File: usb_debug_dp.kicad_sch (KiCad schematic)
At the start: 141 parts, among them J7 Tag-Connect_TC2050-IDC-NL_2x5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, J8 USB-C_GCT_USB4105-GF-A, J9 USB-C_Amphenol_12401598E4, Q12 PJE138K, U29 W25Q80DV_USON, U30 TPS65988DHRSHR, U31 NTS0102_XSON, U32 NCP730BMT330_WSON, U33 TUSB1046-DCIRNQ, U34 FT230X_QFN, U35 AP22615A_TSOT26, U36 TPD4E05U06QDQARQ1, U37 TPD4E05U06QDQARQ1, U38 TPD4E05U06QDQARQ1, U39 TPS65988DHRSHR, U40 AP22615A_TSOT26, U41 TPD4E05U06QDQARQ1, U42 TPD4E05U06QDQARQ1

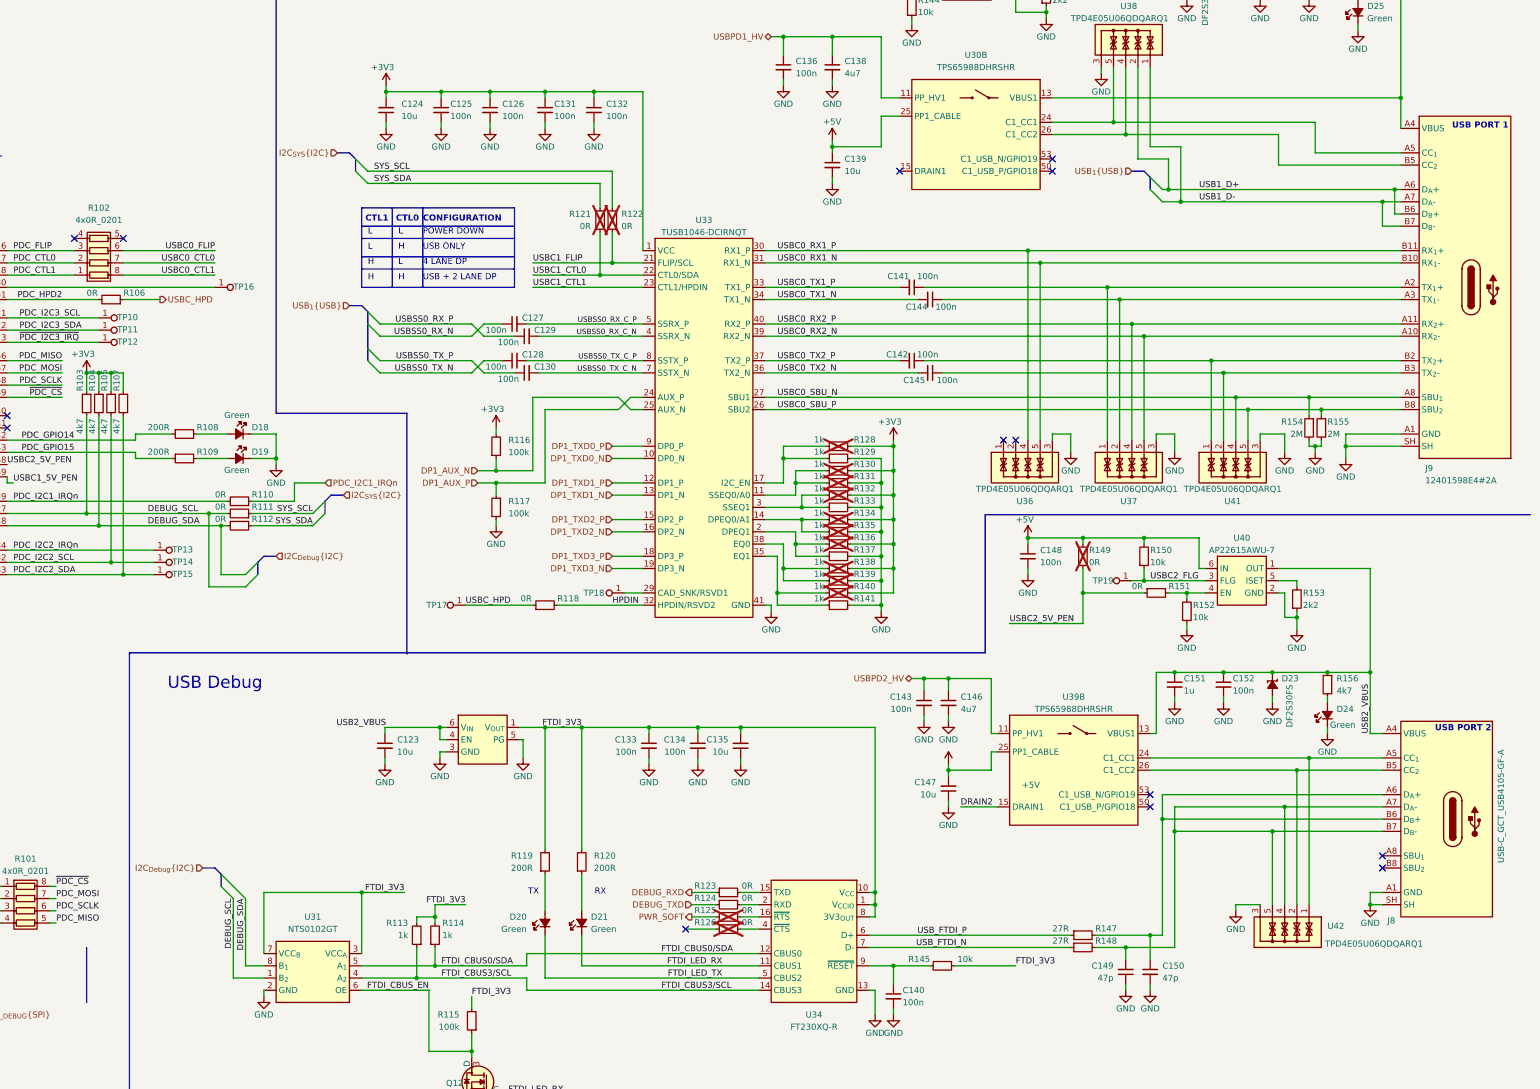
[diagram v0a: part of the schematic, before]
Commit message: [#82847] Prepare current state of schematic to merge with mockup
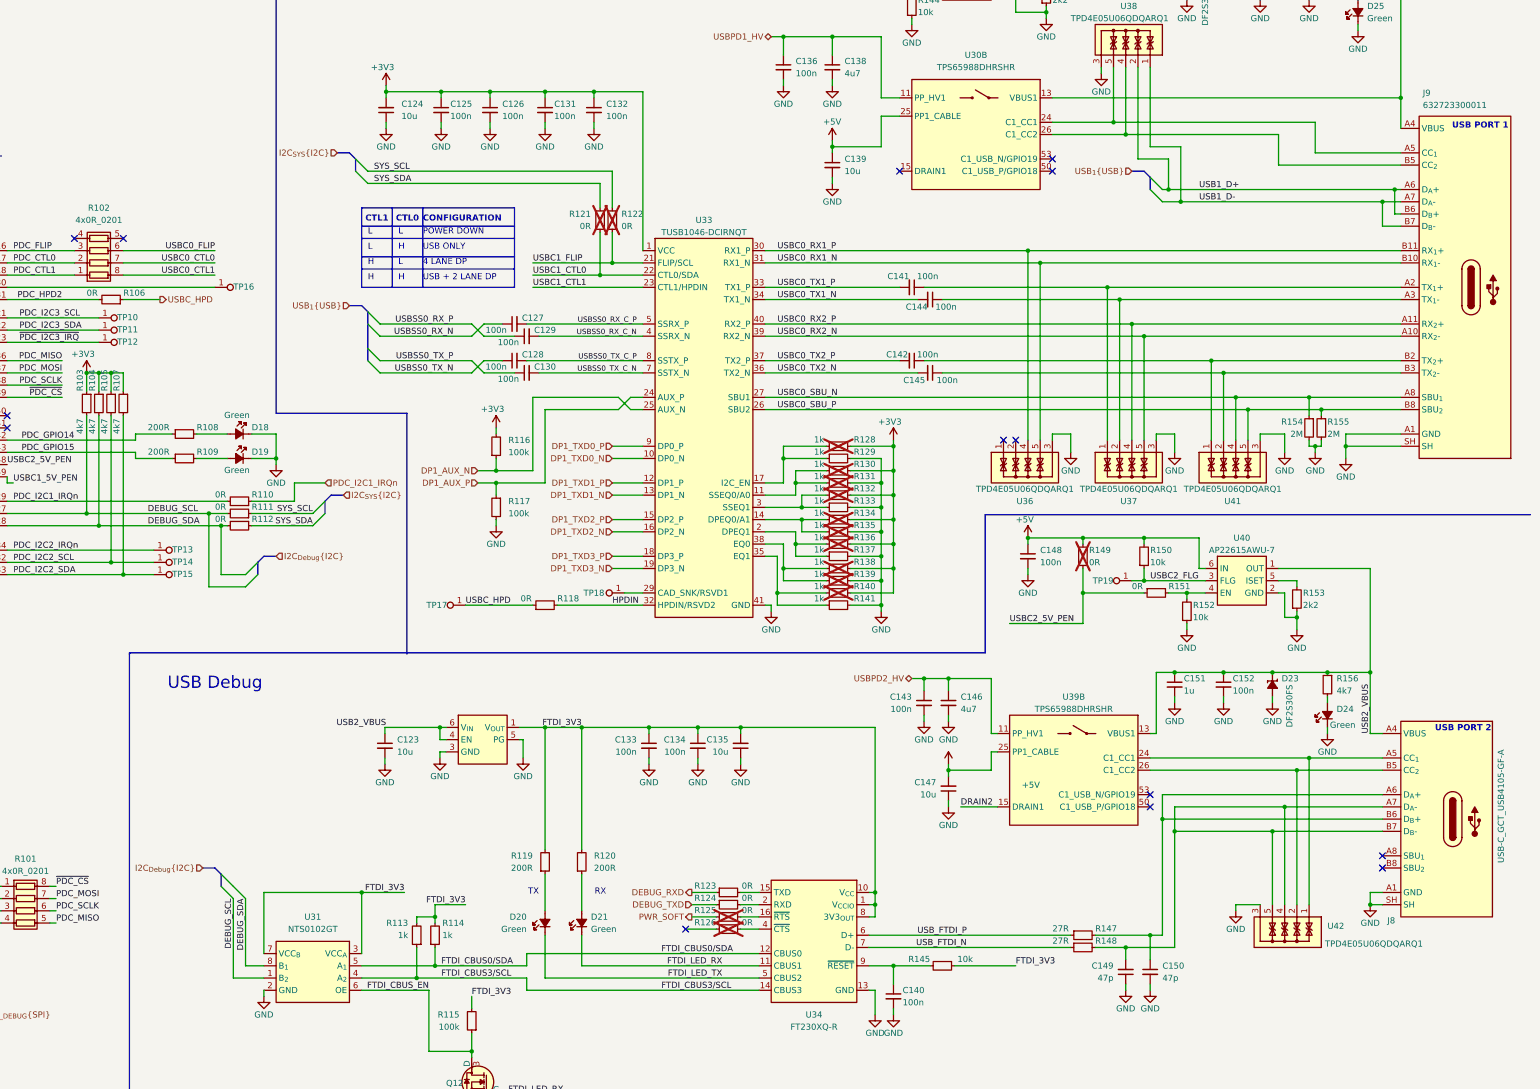
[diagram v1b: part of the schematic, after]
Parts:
- removed J9: USB-C_Amphenol_12401598E4, antmicro-footprints:USB-C_Receptacle_Amphenol_12401598E4, symbol antmicroUSBConnectors:USB-C_Amphenol_12401598E4
- added J9: USB-C_WE_632723300011, antmicro-footprints:USB-C_Receptacle_WE_632723300011, symbol antmicroUSBConnectors:USB-C_WE_632723300011
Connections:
- net GND: now also J9.A1 (GND), J9.A12 (GND), J9.B1 (GND), J9.B12 (GND), J9.SH
- net USB1_D+: now also J9.A6 (D_{A}+), J9.B6 (D_{B}+)
- net USB1_D-: now also J9.A7 (D_{A}-), J9.B7 (D_{B}-)
- net USBC0_RX1_N: now also J9.B10 (RX_{1}-)
- net USBC0_RX1_P: now also J9.B11 (RX_{1}+)
- net USBC0_RX2_N: now also J9.A10 (RX_{2}-)
- net USBC0_RX2_P: now also J9.A11 (RX_{2}+)
- net USBC0_SBU_N: now also J9.A8 (SBU_{1})
- net USBC0_SBU_P: now also J9.B8 (SBU_{2})
- net at C142.1, U41.1, U41.10: now also J9.B2 (TX_{2}+)
- net at C145.1, U41.2, U41.9: now also J9.B3 (TX_{2}-)
- net at C153.1, C154.2, D22.1 (C)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: now also J9.A4 (VBUS), J9.A9 (VBUS), J9.B4 (VBUS), J9.B9 (VBUS)
- net at U30.24 (C1_CC1), U38.5, U38.6: now also J9.A5 (CC_{1})
- net at U30.26 (C1_CC2), U38.4, U38.7: now also J9.B5 (CC_{2})
- net at C141.1, U37.1, U37.10: now also J9.A2 (TX_{1}+)
- net at C144.1, U37.2, U37.9: now also J9.A3 (TX_{1}-)

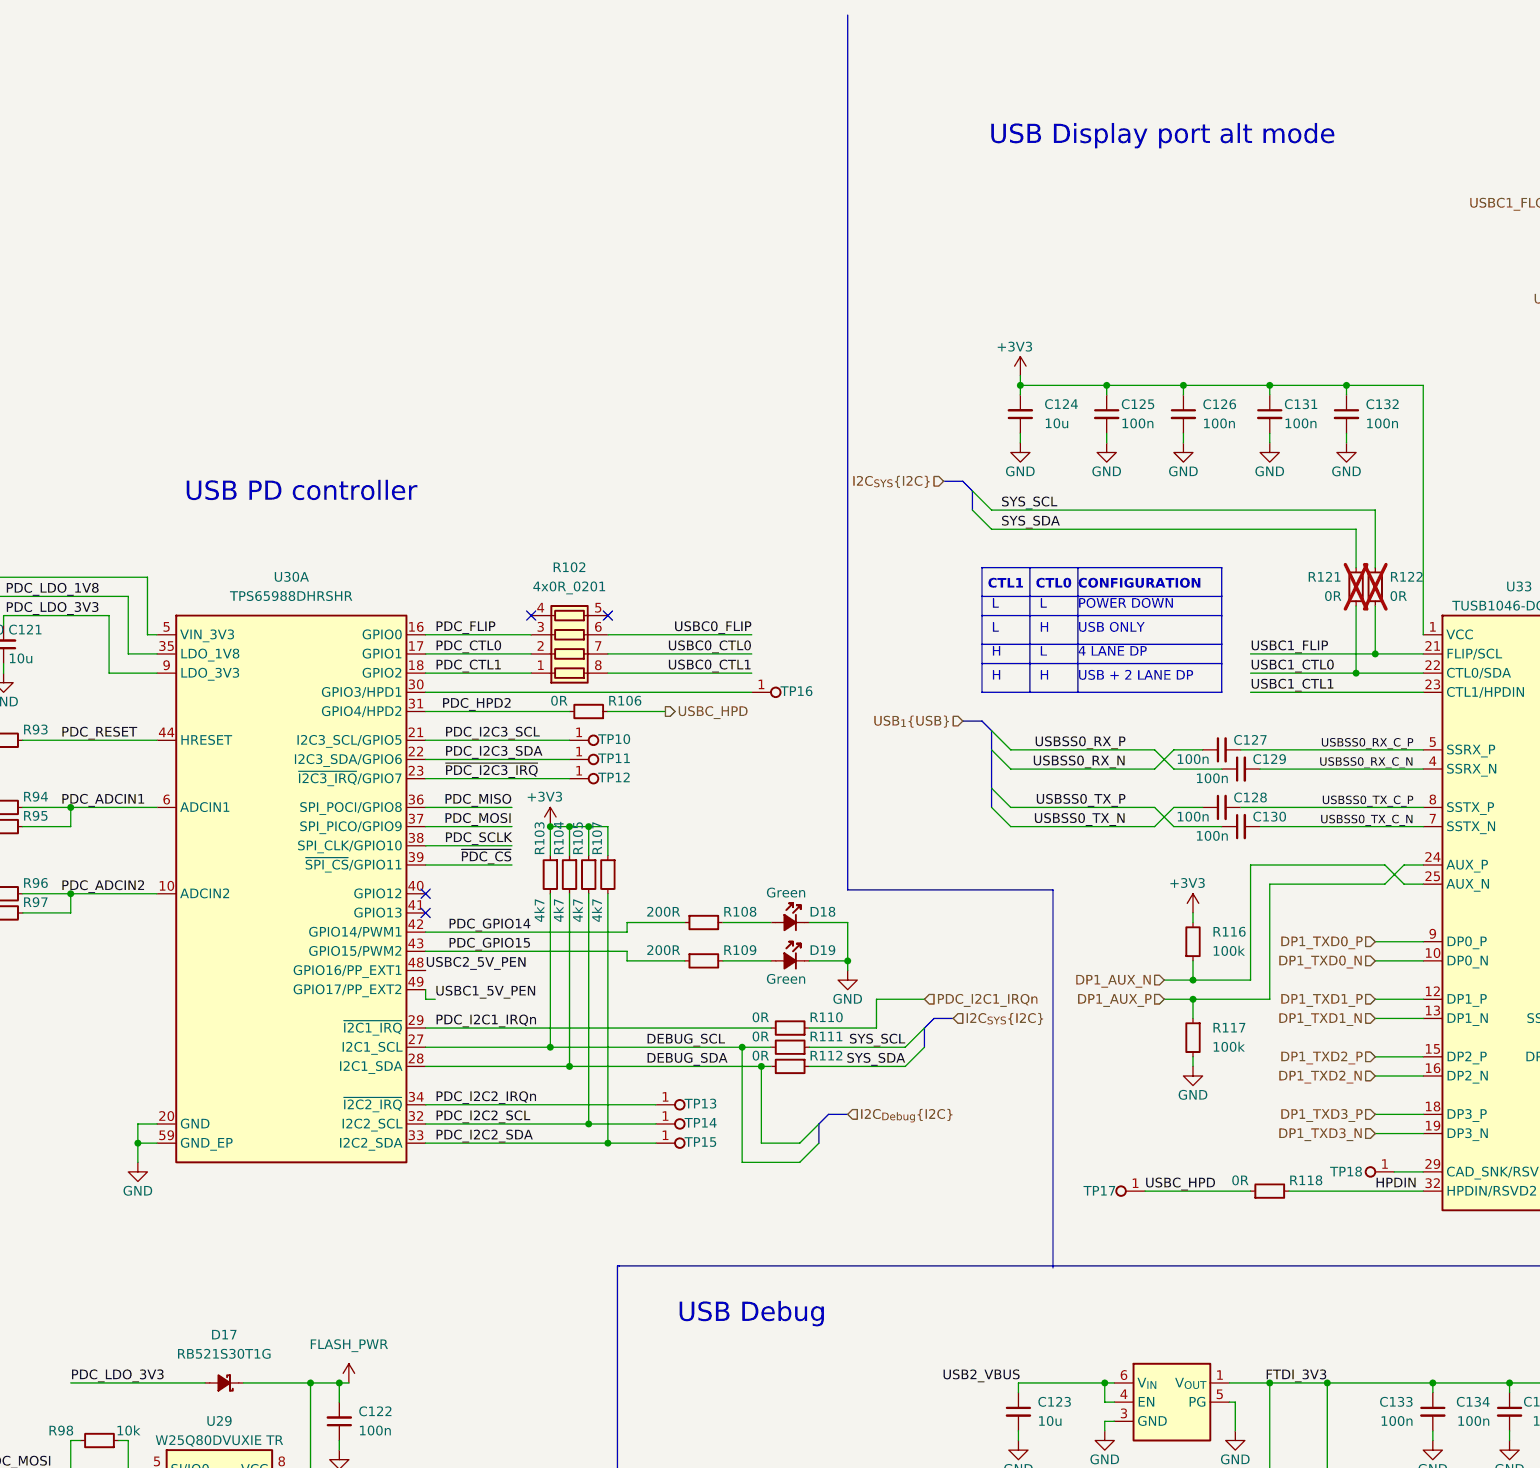
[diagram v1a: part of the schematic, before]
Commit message: [#82837] Standardise sheet sections text size
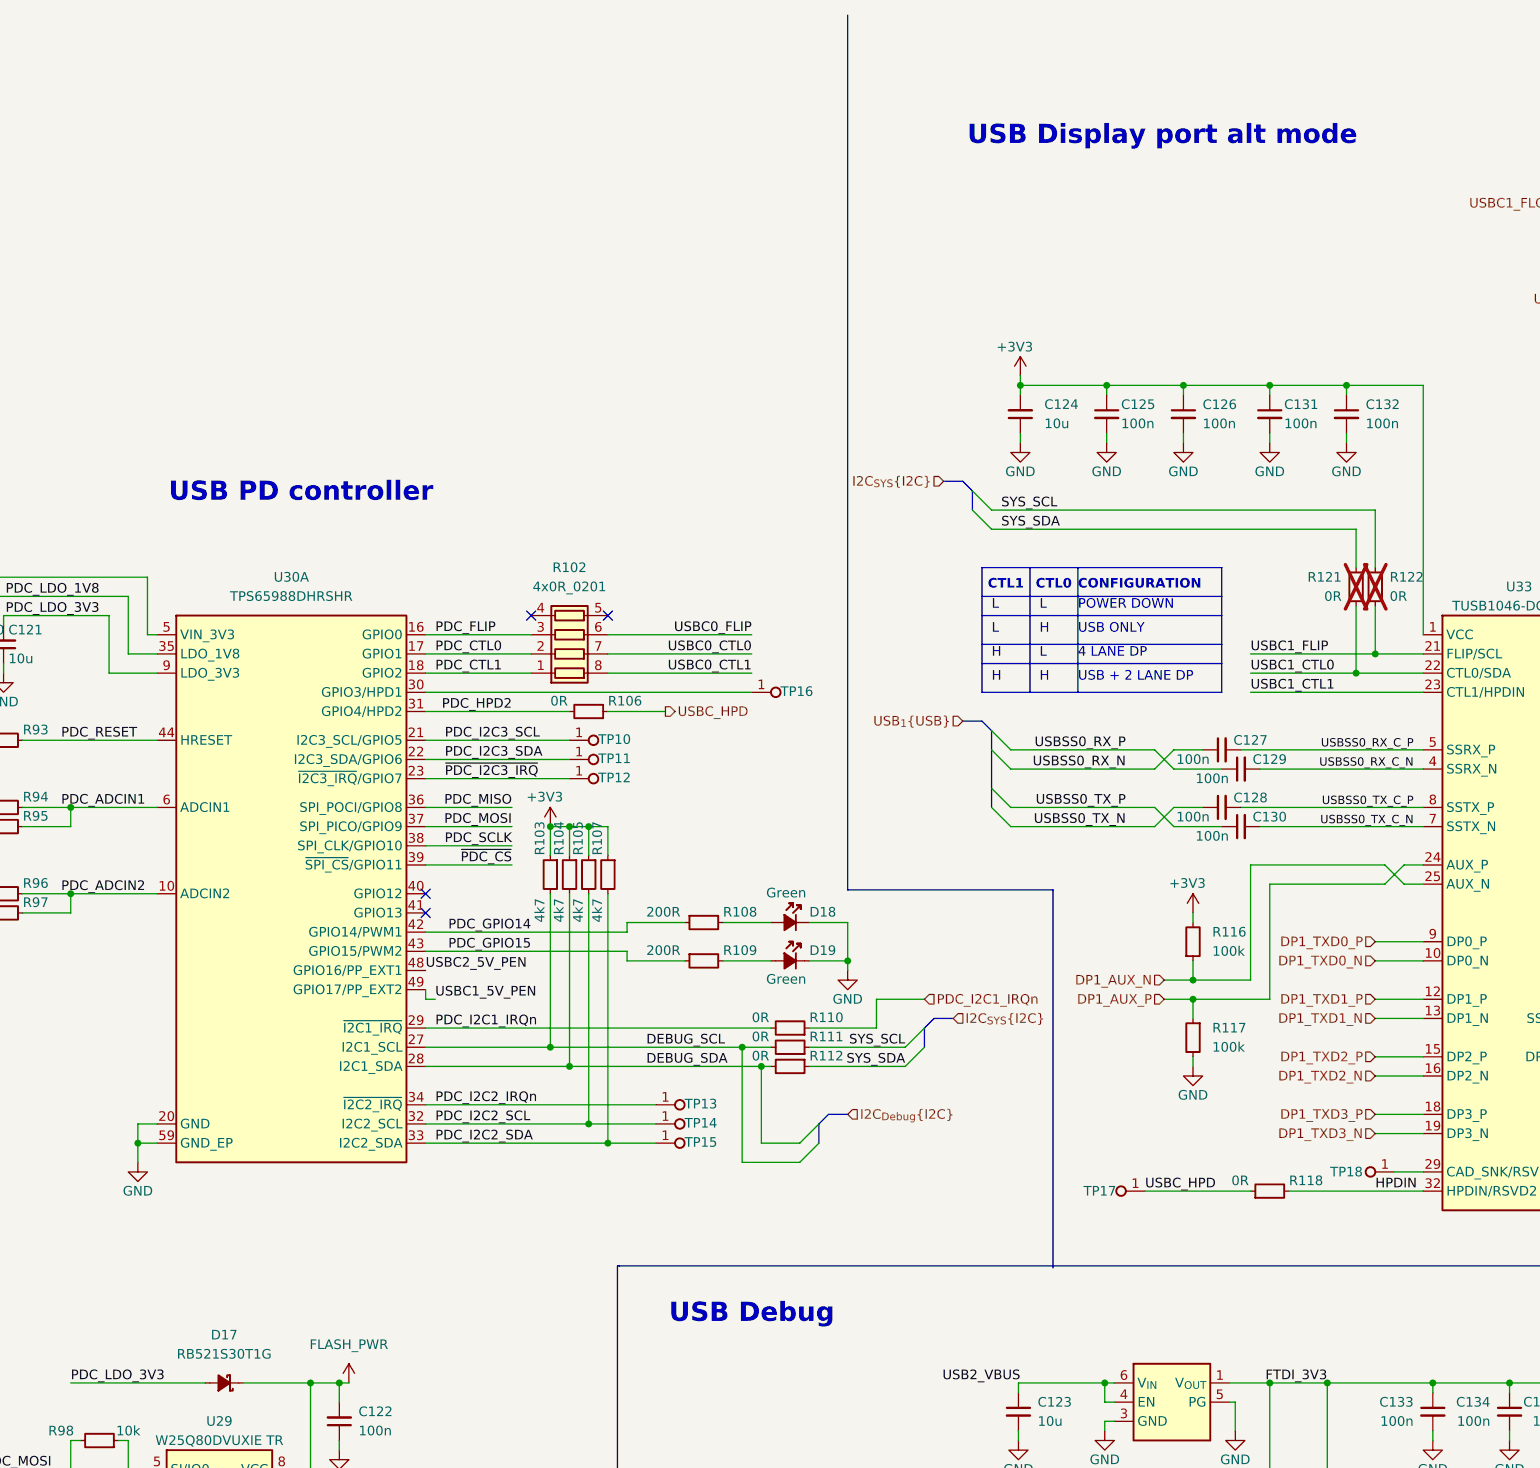
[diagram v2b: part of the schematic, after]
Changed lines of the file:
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@@
 			(font
 				(size 2.54 2.54)
+				(thickness 0.508)
+				(bold yes)
 			)
 		)
@@
 			(font
 				(size 2.54 2.54)
+				(thickness 0.508)
+				(bold yes)
 			)
 		)
@@
 			(font
 				(size 2.54 2.54)
+				(thickness 0.508)
+				(bold yes)
 			)
 		)

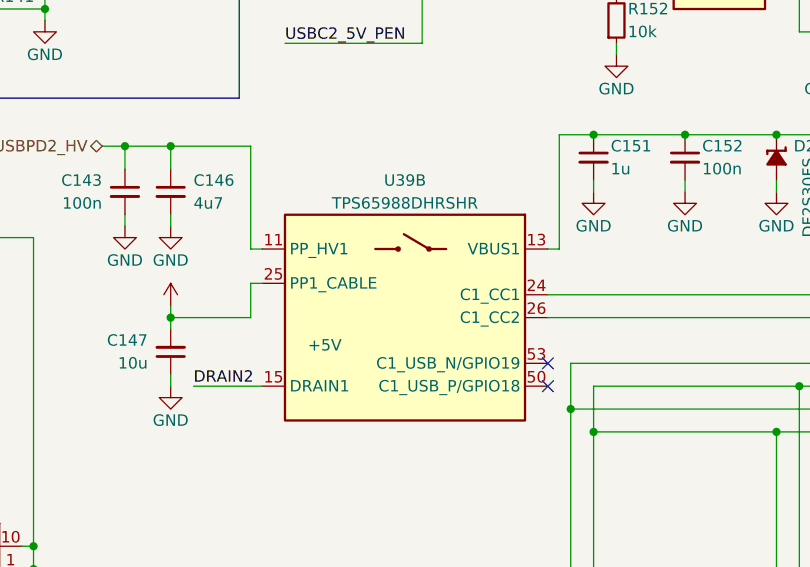
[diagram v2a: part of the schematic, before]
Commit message: [#82837] Reorganize project: split each USB subsheet into two subsheets
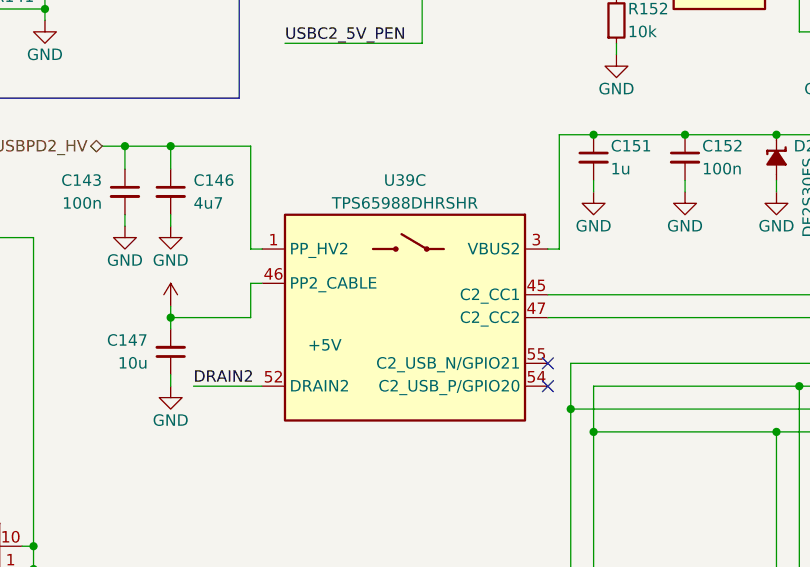
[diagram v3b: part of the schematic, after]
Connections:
- net +5V: now also U39.46 (PP2_CABLE); no longer U39.25 (PP1_CABLE)
- net DRAIN2: now also U39.52 (DRAIN2), U39.56 (DRAIN2), U39.57 (DRAIN2), U39.7 (DRAIN2); no longer U39.15 (DRAIN1), U39.19 (DRAIN1), U39.58 (DRAIN1), U39.8 (DRAIN1)
- net USB2_VBUS: now also U39.3 (VBUS2); no longer U39.13 (VBUS1)
- net USBPD2_HV: now also U39.1 (PP_HV2); no longer U39.11 (PP_HV1)
- net at J8.A5 (CC_{1}), U42.1, U42.10: now also U39.45 (C2_CC1); no longer U39.24 (C1_CC1)
- net at J8.B5 (CC_{2}), U42.2, U42.9: now also U39.47 (C2_CC2); no longer U39.26 (C1_CC2)
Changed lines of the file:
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@@
 		(at 328.93 194.31 0)
 		(mirror y)
-		(unit 2)
+		(unit 3)
 		(exclude_from_sim no)
 		(in_bom yes)
@@
 				(path "/f569b0be-0afd-48b7-93ee-28582a4c645c/12c19ba5-8fdc-4775-a33b-e8b1ade01b0a"
 					(reference "U39")
-					(unit 2)
-				)
-			)
+					(unit 3)
+				)
+			)
